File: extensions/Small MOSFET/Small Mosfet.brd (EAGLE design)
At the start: 26 x 26 mm, 9 parts

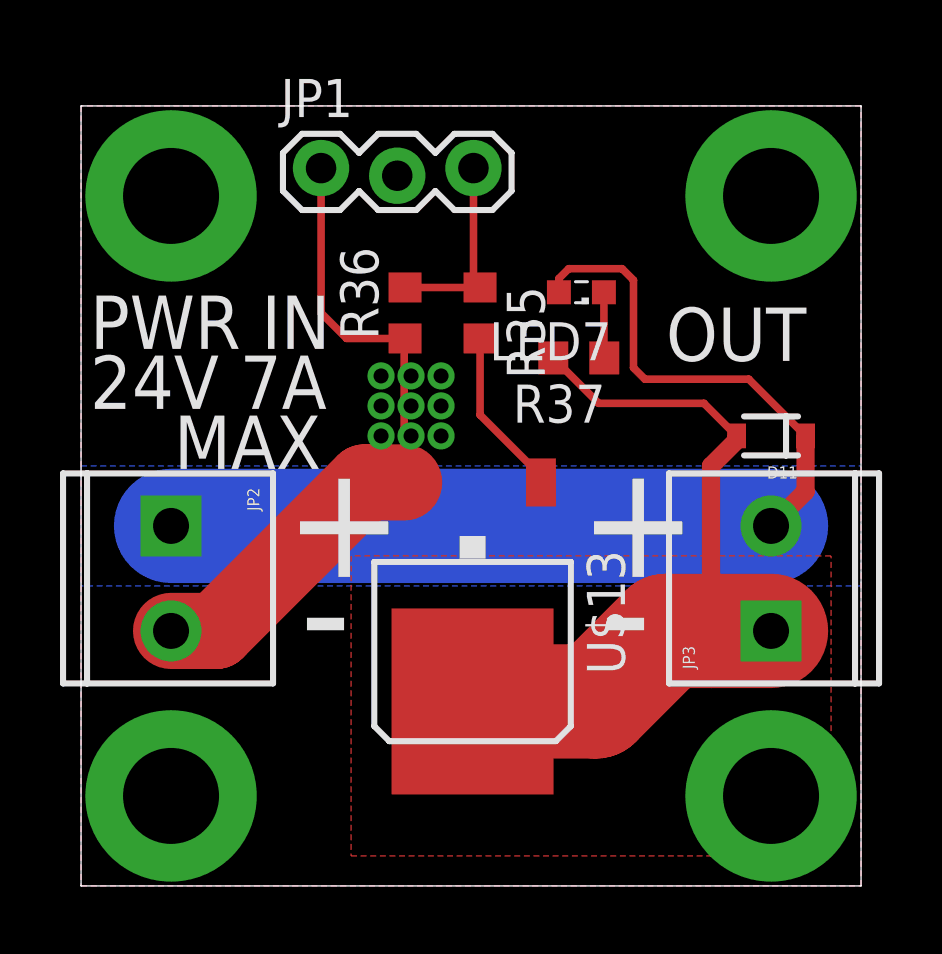
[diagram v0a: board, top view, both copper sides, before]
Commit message: Ray added *final* Small and Large MOSFET extension boards
Just eagle files and CAM for OSHPark for now.
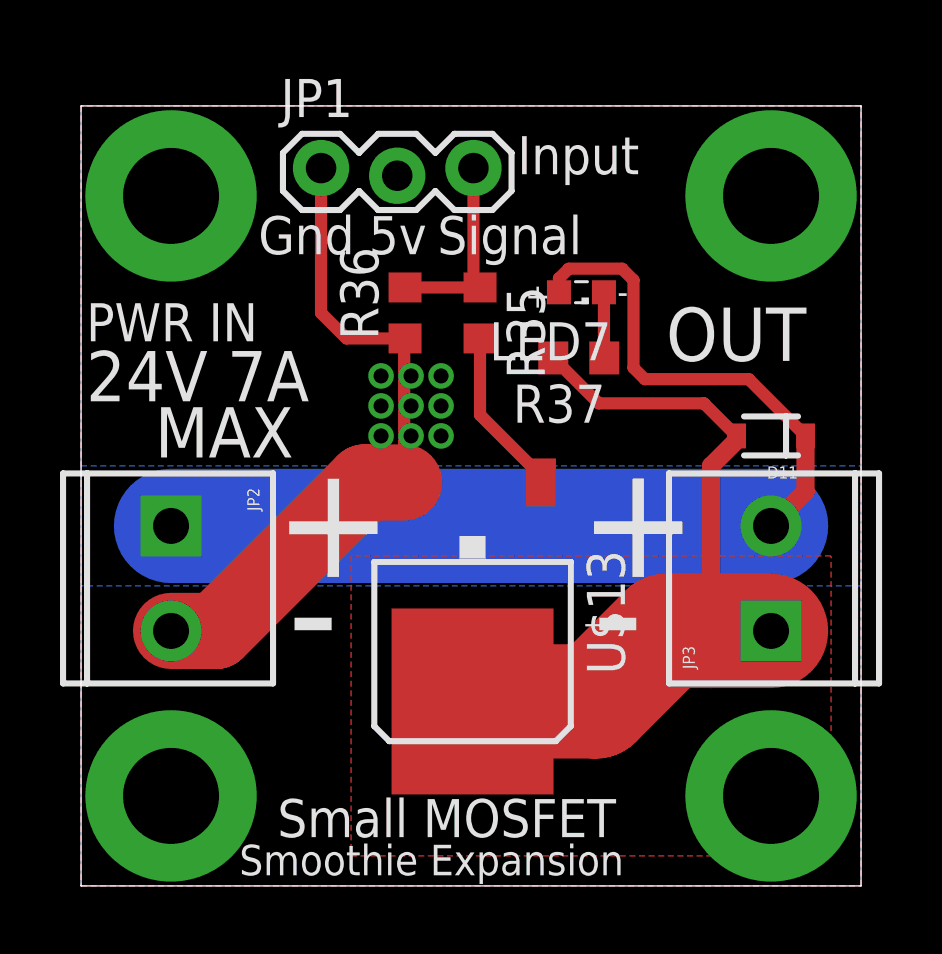
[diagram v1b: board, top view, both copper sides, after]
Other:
- board text added: "24V"
- board text added: "5v"
- board text added: "7A"
- board text added: "Designed by"
- board text added: "Gnd"
- board text added: "Input"
- board text added: "Ray Kholodovsky"
- board text added: "Signal"
- board text added: "Small MOSFET"
- board text added: "Smoothie Expansion"
- board text removed: "24V 7A"
